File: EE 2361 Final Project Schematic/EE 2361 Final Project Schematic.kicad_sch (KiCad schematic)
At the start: 1 part

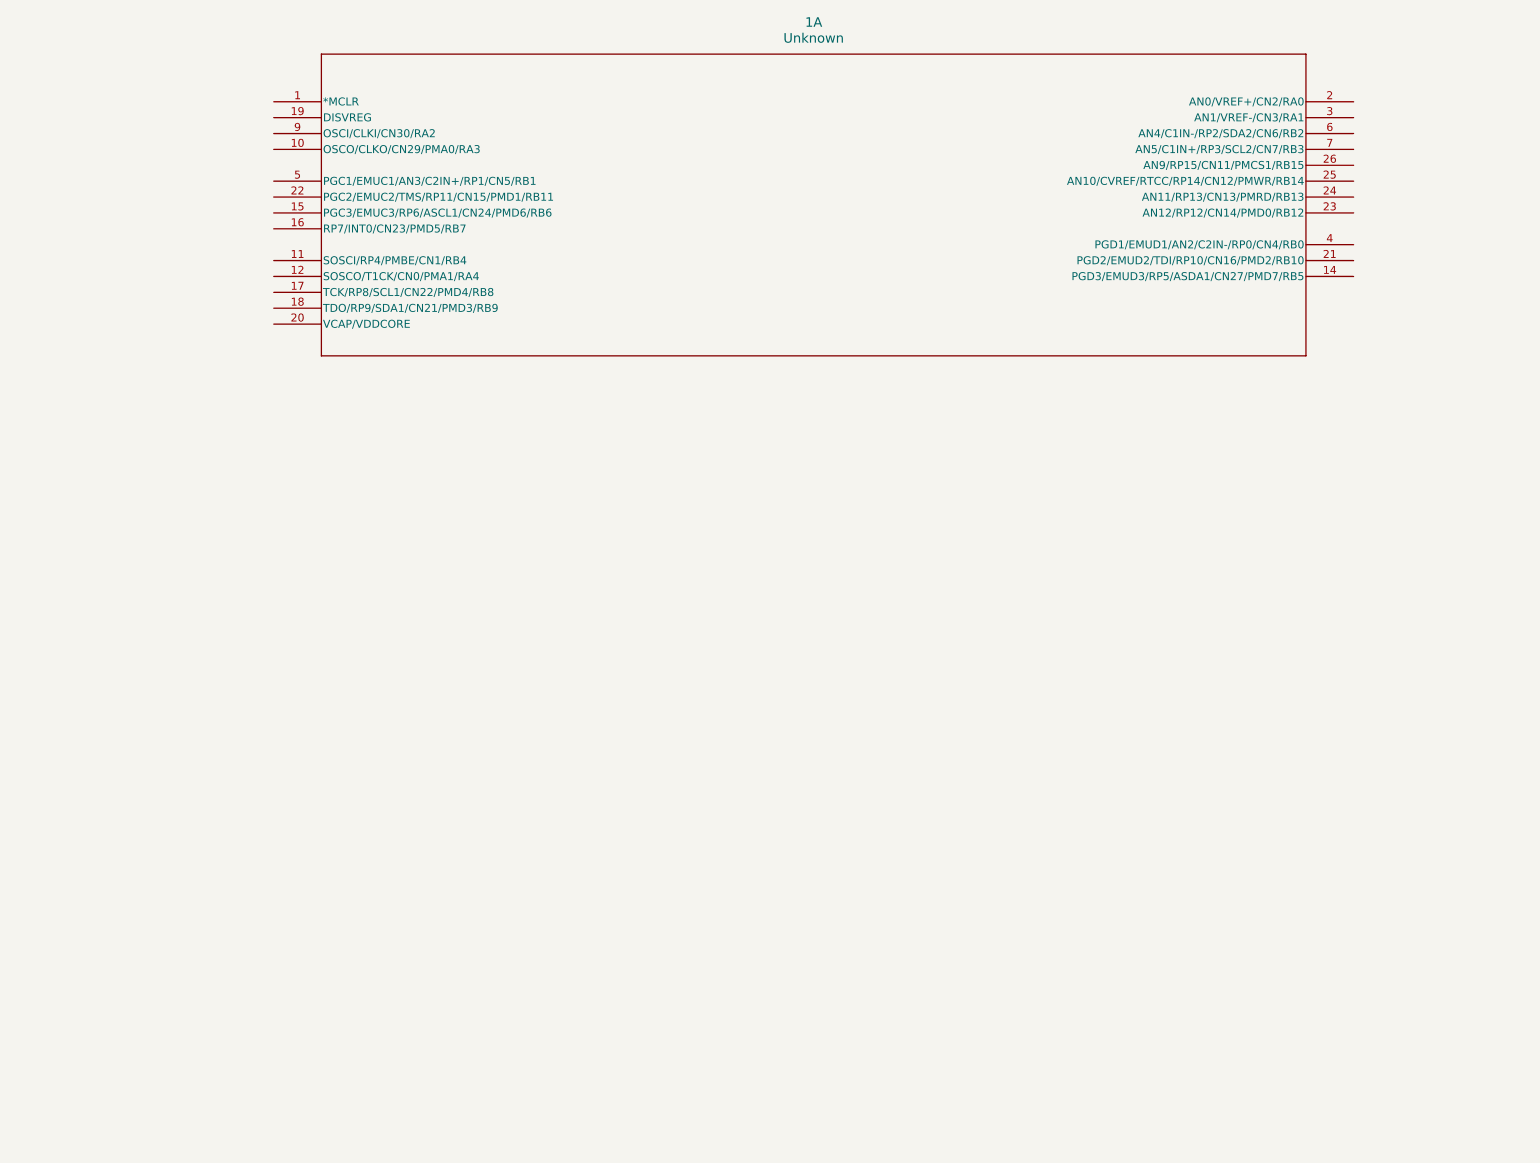
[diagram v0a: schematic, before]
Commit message: Schematic v1 Revision Completed
If pins are being changed to digital, the header tags might want to be renamed.

There are no power pins on the schematic diagram, and as such its presumed to have those pins operating as normal.
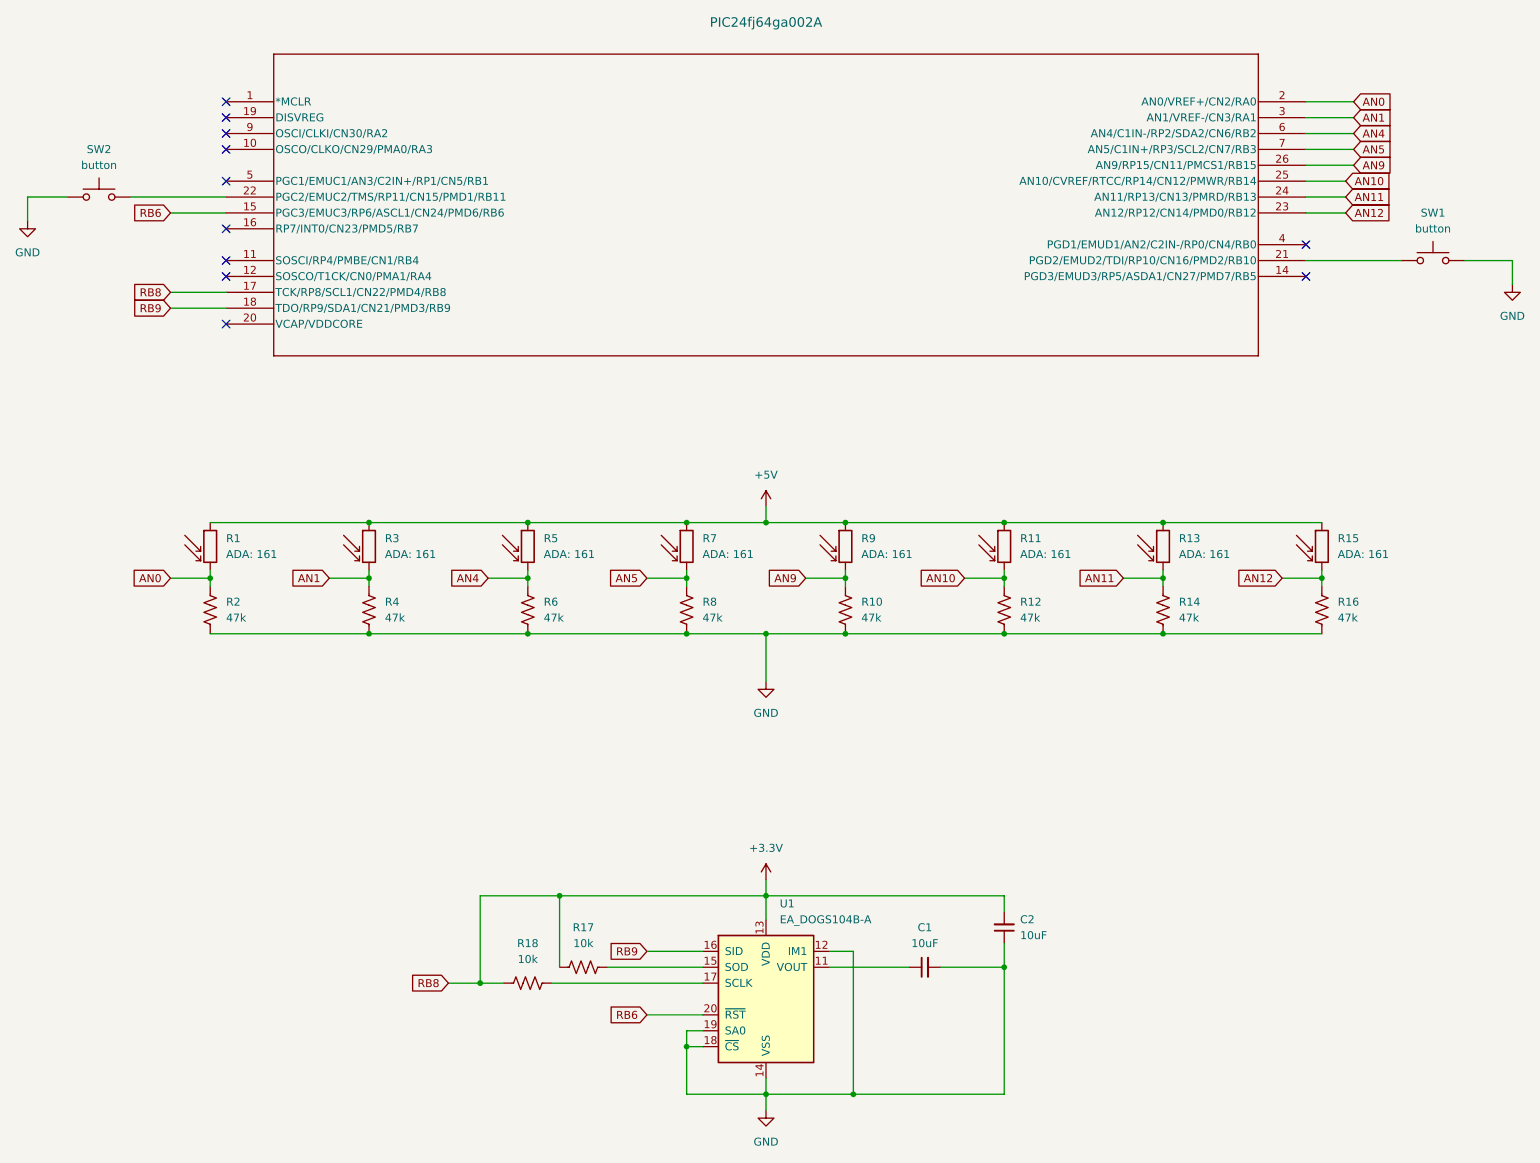
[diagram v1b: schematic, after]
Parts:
- added C1, C2: 10uF, symbol Device:C_Small
- added R1, R11, R13, R15, R3, R5, R7, R9: ADA: 161, symbol Device:R_Photo
- added R10, R12, R14, R16, R2, R4, R6, R8: 47k, symbol Device:R_US
- added R17, R18: 10k, symbol Device:R_US
- added SW1, SW2: button, symbol Switch:SW_Push
- added U1: EA_DOGS104B-A, Display:EA_DOGS104X-A, symbol Display_Graphic:EA_DOGS104B-A
- PIC24fj64ga002: renamed from 1; value Unknown -> ~
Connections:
- net RB6: now reaches PIC24fj64ga002.15 (PGC3/EMUC3/RP6/ASCL1/CN24/PMD6/RB6)
- net RB6: now also U1.20 (~{RST})
- net +3.3V: now reaches PIC24fj64ga002.17 (TCK/RP8/SCL1/CN22/PMD4/RB8)
- net +3.3V: now also C2.2, R17.1, R18.1, U1.13 (VDD)
- net RB9: now reaches PIC24fj64ga002.18 (TDO/RP9/SDA1/CN21/PMD3/RB9)
- net RB9: now also U1.16 (SID)
- net AN0: now reaches PIC24fj64ga002.2 (AN0/VREF+/CN2/RA0)
- net AN0: now also R1.2, R2.1
- net at PIC24fj64ga002.21 (PGD2/EMUD2/TDI/RP10/CN16/PMD2/RB10): now also SW1.1
- net at PIC24fj64ga002.22 (PGC2/EMUC2/TMS/RP11/CN15/PMD1/RB11): now also SW2.2
- net AN12: now reaches PIC24fj64ga002.23 (AN12/RP12/CN14/PMD0/RB12)
- net AN12: now also R15.2, R16.1
- net AN11: now reaches PIC24fj64ga002.24 (AN11/RP13/CN13/PMRD/RB13)
- net AN11: now also R13.2, R14.1
- net AN10: now reaches PIC24fj64ga002.25 (AN10/CVREF/RTCC/RP14/CN12/PMWR/RB14)
- net AN10: now also R11.2, R12.1
- net AN9: now reaches PIC24fj64ga002.26 (AN9/RP15/CN11/PMCS1/RB15)
- net AN9: now also R10.1, R9.2
- net AN1: now reaches PIC24fj64ga002.3 (AN1/VREF-/CN3/RA1)
- net AN1: now also R3.2, R4.1
- net AN4: now reaches PIC24fj64ga002.6 (AN4/C1IN-/RP2/SDA2/CN6/RB2)
- net AN4: now also R5.2, R6.1
- net AN5: now reaches PIC24fj64ga002.7 (AN5/C1IN+/RP3/SCL2/CN7/RB3)
- net AN5: now also R7.2, R8.1
- new net: C1.1, U1.11 (VOUT)
- new net: R17.2, U1.15 (SOD)
- new net: R18.2, U1.17 (SCLK)
- new net +5V: R1.1, R11.1, R13.1, R15.1, R3.1, R5.1, R7.1, R9.1
- new net GND: C1.2, C2.1, R10.2, R12.2, R14.2, R16.2, R2.2, R4.2, R6.2, R8.2, SW1.2, SW2.1, U1.12 (IM1), U1.14 (VSS), U1.18 (~{CS}), U1.19 (SA0)
- no-connect marks 0 -> 11
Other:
- company: (none) -> A. Ecoff, D. Gomez, C. Harper, D. Hamilton
- title: (none) -> EE 2361 Final Project Schematic
- moved on the sheet: PIC24fj64ga002A

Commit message: Updated PIC Circuitry
More documentation document edits
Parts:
- added C3: 10uF, symbol Device:C_Small
- added R19: 10k, symbol Device:R_US
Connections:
- net +3.3V: now also R19.1
- net GND: now also C3.2
- net at PIC24fj64ga002.1 (*MCLR): now also R19.2
- net at PIC24fj64ga002.20 (VCAP/VDDCORE): now also C3.1
- no-connect marks 11 -> 9

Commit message: Finished KiCad Schematic
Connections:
- net AN0 renamed RA0
- net AN1 renamed RA1
- net AN10 renamed RB14
- net AN11 renamed RB13
- net AN12 renamed RB12
- net AN4 renamed RB2
- net AN5 renamed RB3
- net AN9 renamed RB15
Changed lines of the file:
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@@
 		(title "EE 2361 Final Project Schematic")
 		(date "2025-04-20")
-		(rev "2")
+		(rev "3")
 		(company "A. Ecoff, D. Gomez, C. Harper, D. Hamilton")
 	)
@@
 	(wire
 		(pts
+			(xy 226.06 57.15) (xy 232.41 57.15)
+		)
+		(stroke
+			(width 0)
+			(type default)
+		)
+	)
+	(wire
+		(pts
 			(xy 177.8 114.3) (xy 203.2 114.3)
 		)
@@
 	(wire
 		(pts
-			(xy 226.06 57.15) (xy 233.68 57.15)
-		)
-		(stroke
-			(width 0)
-			(type default)
-		)
-	)
-	(wire
-		(pts
 			(xy 127 132.08) (xy 139.7 132.08)
 		)
@@
 		)
 	)
-	(global_label "AN9"
+	(label "Photoresistor Array"
+		(at 119.38 102.87 0)
+		(fields_autoplaced yes)
+		(effects
+			(font
+				(size 3 3)
+				(thickness 0.8)
+				(bold yes)
+			)
+			(justify left bottom)
+		)
+	)
+	(label "I2C LCD"
+		(at 132.08 161.29 0)
+		(fields_autoplaced yes)
+		(effects
+			(font
+				(size 3 3)
+				(thickness 0.6)
+				(bold yes)
+			)
+			(justify left bottom)
+		)
+	)
+	(global_label "RB15"
 		(shape input)
 		(at 146.05 123.19 180)
@@
 		)
 		(property "Intersheetrefs" "${INTERSHEET_REFS}"
-			(at 139.4362 123.19 0)
+			(at 138.1058 123.19 0)
 			(effects
 				(font
@@
 		)
 	)
-	(global_label "AN5"
+	(global_label "RB3"
 		(shape input)
 		(at 233.68 54.61 0)
@@
 		)
 		(property "Intersheetrefs" "${INTERSHEET_REFS}"
-			(at 240.2938 54.61 0)
+			(at 240.4147 54.61 0)
 			(effects
 				(font
@@
 		)
 	)
-	(global_label "AN0"
+	(global_label "RA0"
 		(shape input)
 		(at 233.68 46.99 0)
@@
 		)
 		(property "Intersheetrefs" "${INTERSHEET_REFS}"
-			(at 240.2938 46.99 0)
+			(at 240.2333 46.99 0)
 			(effects
 				(font
@@
 		)
 	)
-	(global_label "AN10"
+	(global_label "RB14"
 		(shape input)
 		(at 171.45 123.19 180)
@@
 		)
 		(property "Intersheetrefs" "${INTERSHEET_REFS}"
-			(at 163.6267 123.19 0)
+			(at 163.5058 123.19 0)
 			(effects
 				(font
@@
 		)
 	)
-	(global_label "AN9"
-		(shape input)
-		(at 233.68 57.15 0)
+	(global_label "RB15"
+		(shape input)
+		(at 232.41 57.15 0)
 		(fields_autoplaced yes)
 		(effects
@@
 		)
 		(property "Intersheetrefs" "${INTERSHEET_REFS}"
-			(at 240.2938 57.15 0)
+			(at 240.3542 57.15 0)
 			(effects
 				(font
@@
 		)
 	)
-	(global_label "AN10"
+	(global_label "RB14"
 		(shape input)
 		(at 232.41 59.69 0)
@@
 		)
 		(property "Intersheetrefs" "${INTERSHEET_REFS}"
-			(at 240.2333 59.69 0)
+			(at 240.3542 59.69 0)
 			(effects
 				(font
@@
 		)
 	)
-	(global_label "AN12"
+	(global_label "RB12"
 		(shape input)
 		(at 232.41 64.77 0)
@@
 		)
 		(property "Intersheetrefs" "${INTERSHEET_REFS}"
-			(at 240.2333 64.77 0)
+			(at 240.3542 64.77 0)
 			(effects
 				(font
@@
 		)
 	)
-	(global_label "AN0"
+	(global_label "RA0"
 		(shape input)
 		(at 44.45 123.19 180)
@@
 		)
 		(property "Intersheetrefs" "${INTERSHEET_REFS}"
-			(at 37.8362 123.19 0)
+			(at 37.8967 123.19 0)
 			(effects
 				(font
@@
 		)
 	)
-	(global_label "AN5"
+	(global_label "RB3"
 		(shape input)
 		(at 120.65 123.19 180)
@@
 		)
 		(property "Intersheetrefs" "${INTERSHEET_REFS}"
-			(at 114.0362 123.19 0)
+			(at 113.9153 123.19 0)
 			(effects
 				(font
@@
 		)
 	)
-	(global_label "AN4"
+	(global_label "RB2"
 		(shape input)
 		(at 233.68 52.07 0)
@@
 		)
 		(property "Intersheetrefs" "${INTERSHEET_REFS}"
-			(at 240.2938 52.07 0)
+			(at 240.4147 52.07 0)
 			(effects
 				(font
@@
 		)
 	)
-	(global_label "AN11"
+	(global_label "RB13"
 		(shape input)
 		(at 196.85 123.19 180)
@@
 		)
 		(property "Intersheetrefs" "${INTERSHEET_REFS}"
-			(at 189.0267 123.19 0)
+			(at 188.9058 123.19 0)
 			(effects
 				(font
@@
 		)
 	)
-	(global_label "AN11"
+	(global_label "RB13"
 		(shape input)
 		(at 232.41 62.23 0)
@@
 		)
 		(property "Intersheetrefs" "${INTERSHEET_REFS}"
-			(at 240.2333 62.23 0)
+			(at 240.3542 62.23 0)
 			(effects
 				(font
@@
 		)
 	)
-	(global_label "AN4"
+	(global_label "RB2"
 		(shape input)
 		(at 95.25 123.19 180)
@@
 		)
 		(property "Intersheetrefs" "${INTERSHEET_REFS}"
-			(at 88.6362 123.19 0)
+			(at 88.5153 123.19 0)
 			(effects
 				(font
@@
 		)
 	)
-	(global_label "AN12"
+	(global_label "RB12"
 		(shape input)
 		(at 222.25 123.19 180)
@@
 		)
 		(property "Intersheetrefs" "${INTERSHEET_REFS}"
-			(at 214.4267 123.19 0)
+			(at 214.3058 123.19 0)
 			(effects
 				(font
@@
 		)
 	)
-	(global_label "AN1"
+	(global_label "RA1"
 		(shape input)
 		(at 69.85 123.19 180)
@@
 		)
 		(property "Intersheetrefs" "${INTERSHEET_REFS}"
-			(at 63.2362 123.19 0)
+			(at 63.2967 123.19 0)
 			(effects
 				(font
@@
 		)
 	)
-	(global_label "AN1"
+	(global_label "RA1"
 		(shape input)
 		(at 233.68 49.53 0)
@@
 		)
 		(property "Intersheetrefs" "${INTERSHEET_REFS}"
-			(at 240.2938 49.53 0)
-			(effects
-				(font
+			(at 240.2333 49.53 0)
+			(effects
+				(font

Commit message: Updated Schematic + Program Info
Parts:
- R10, R12, R14, R16, R2, R4, R6, R8: value 47k -> 1k
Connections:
- net +5V is gone; now on net +3.3V: R1.1, R11.1, R13.1, R15.1, R3.1, R5.1, R7.1, R9.1
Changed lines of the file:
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@@
 			)
 		)
-		(property "Value" "47k"
+		(property "Value" "1k"
 			(at 205.74 129.5399 0)
 			(effects
@@
 			)
 		)
-		(property "Value" "47k"
+		(property "Value" "1k"
 			(at 154.94 129.5399 0)
 			(effects
@@
 			)
 		)
-		(property "Value" "47k"
+		(property "Value" "1k"
 			(at 78.74 129.5399 0)
 			(effects
@@
 			)
 		)
-		(property "Value" "47k"
+		(property "Value" "1k"
 			(at 53.34 129.5399 0)
 			(effects
@@
 			)
 		)
-		(property "Value" "+5V"
+		(property "Value" "+3.3V"
 			(at 139.7 106.68 0)
 			(effects
@@
 			)
 		)
-		(property "Value" "47k"
+		(property "Value" "1k"
 			(at 104.14 129.5399 0)
 			(effects
@@
 			)
 		)
-		(property "Value" "47k"
+		(property "Value" "1k"
 			(at 231.14 129.5399 0)
 			(effects
@@
 			)
 		)
-		(property "Value" "47k"
+		(property "Value" "1k"
 			(at 129.54 129.5399 0)
 			(effects
@@
 			)
 		)
-		(property "Value" "47k"
+		(property "Value" "1k"
 			(at 180.34 129.5399 0)
 			(effects
